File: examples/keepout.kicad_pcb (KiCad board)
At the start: 2 copper layers, 40 x 20 mm, 2 parts

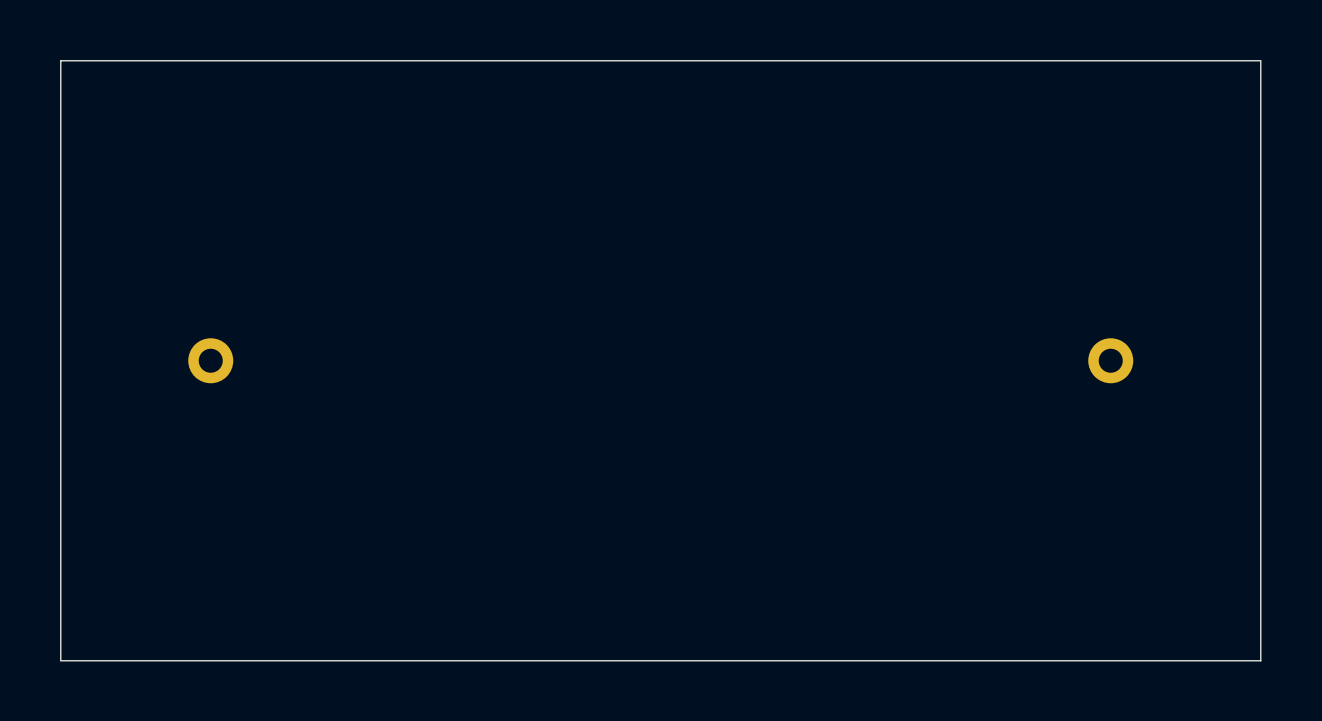
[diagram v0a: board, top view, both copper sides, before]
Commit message: Route around rotated rectangular pads exactly (#20)
Co-authored-by: penguin425 <penguin425@users.noreply.github.com>
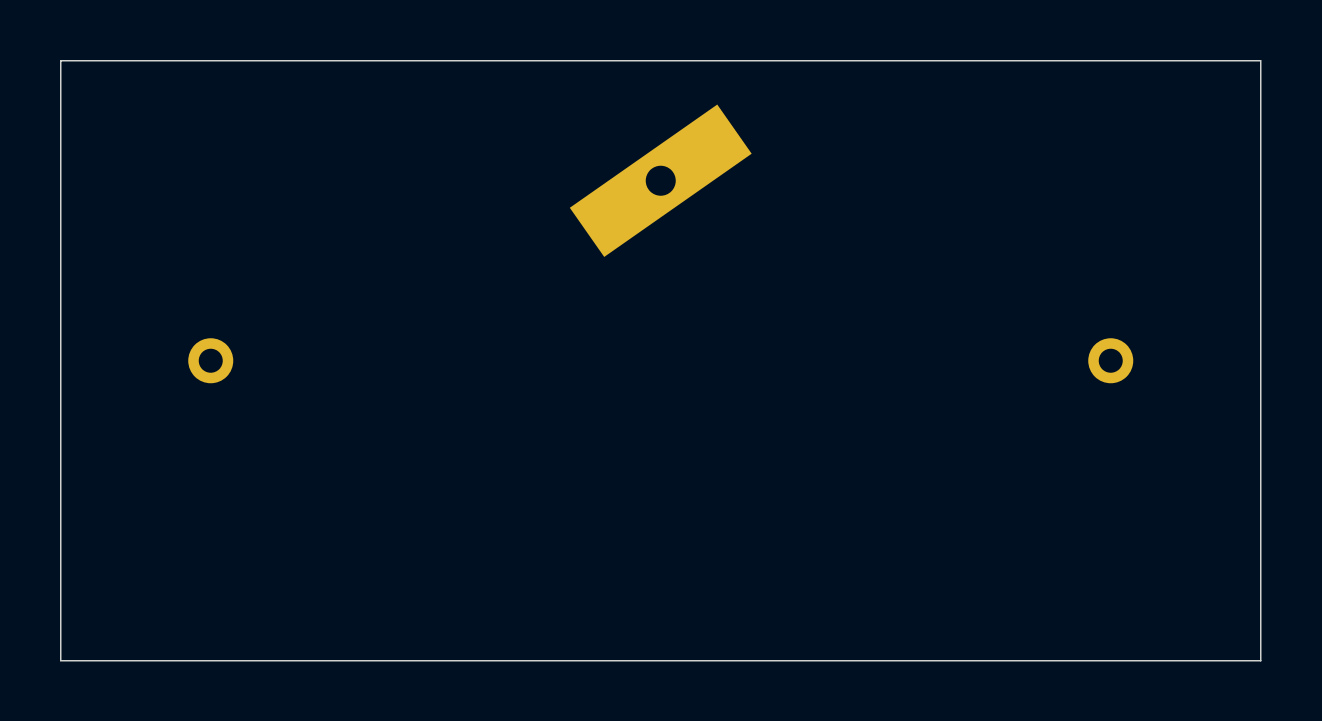
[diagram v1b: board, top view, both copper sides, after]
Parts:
- added ?: , rotated-obstacle, F.Cu at (20.0, 4.00)
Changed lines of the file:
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@@
   (footprint "terminal" (layer "F.Cu") (at 35 10)
     (pad "1" thru_hole circle (at 0 0) (size 1.5 1.5) (drill 0.8) (layers "*.Cu" "*.Mask") (net 1 "SIGNAL")))
+  (footprint "rotated-obstacle" (layer "F.Cu") (at 20 4)
+    (pad "" np_thru_hole rect (at 0 0 35) (size 6 2) (drill 1) (layers "*.Cu" "*.Mask")))
   (zone (net 0) (net_name "") (layer "F.Cu")
     (keepout (tracks not_allowed) (vias not_allowed) (copperpour not_allowed))
